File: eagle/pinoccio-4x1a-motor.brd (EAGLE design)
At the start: 25.4 x 43.2 mm, 3 parts

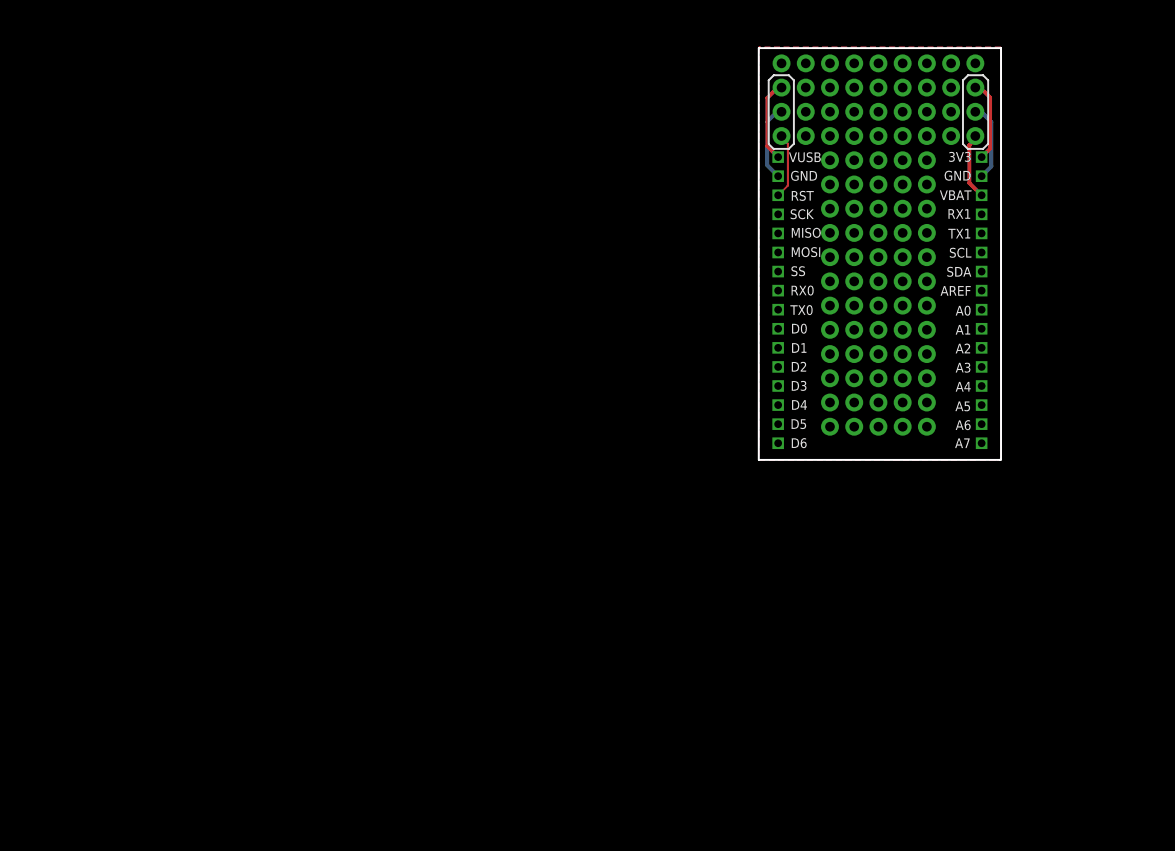
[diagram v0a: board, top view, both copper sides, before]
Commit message: First commit of new shield.
Main components added, no signals.
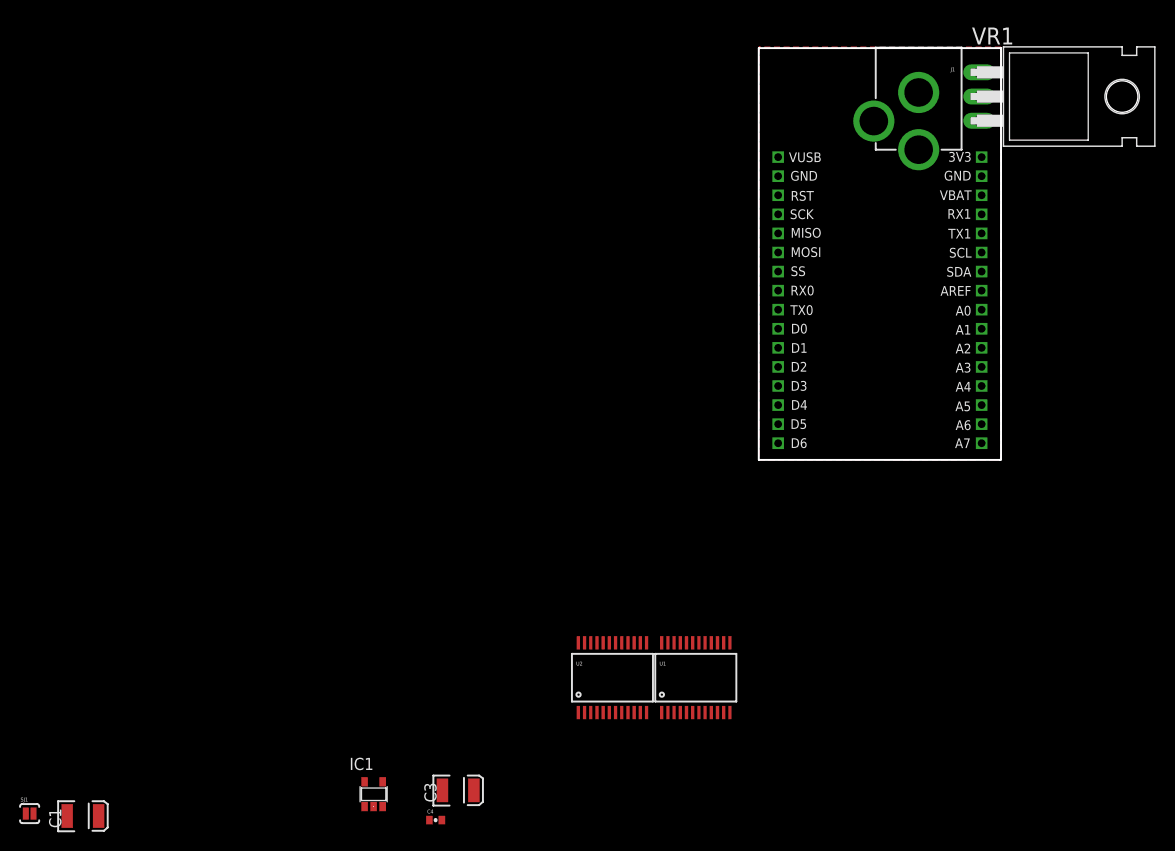
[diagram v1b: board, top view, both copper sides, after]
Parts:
- removed U$1: PROTO, Pinoccio:1X1PROTO
- added C1, C3: 10uf , 20V, SparkFun:EIA3528
- added C4: 0.1uF, SparkFun:0402-CAP
- added IC1: 74LVC1G04DBV, 74xx-little-de:SOT23-5
- added J1: POWER_JACKPTH, SparkFun-Connectors:POWER_JACK_PTH
- added SJ1: SOLDERJUMPERNC2, SparkFun-Passives:SJ_2S-NOTRACE
- added U1, U2: TB6621FNG, SparkFun:SSOP24
- added VR1: LF60ABV, linear:TO220H
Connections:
- new net N$1: C1.A, C3.A, C4.2, VR1.3
- new net N$2: IC1.2, U1.21
- new net N$3: IC1.4, SJ1.1, U1.22
- new net N$4: SJ1.2
- new net VCC: IC1.5
- net GND: now also C1.C, C3.C, C4.1, IC1.3, VR1.1; no longer U$1.53, U$1.77, U$1.P-GND, U$1.P-GND2
- net RESET: no longer U$1.P-RESET
- net VBAT-AE: no longer U$1.P-VBAT
- net VCC-AE: no longer U$1.P-VCC
- net VUSB: no longer U$1.P-VUSB
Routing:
- net GND: track 16.3 -> 0.00 mm
- net VUSB: track 8.62 -> 0.00 mm
- net VCC-AE: track 8.60 -> 0.00 mm
- net VBAT-AE: track 7.01 -> 0.00 mm
- net RESET: track 6.90 -> 0.00 mm
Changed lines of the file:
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@@
 <?xml version="1.0" encoding="utf-8"?>
 <!DOCTYPE eagle SYSTEM "eagle.dtd">
-<eagle version="6.2">
+<eagle version="6.4">
 <drawing>
 <settings>
@@
 <setting verticaltext="up"/>
 </settings>
-<grid distance="1" unitdist="mil" unit="mil" style="lines" multiple="1" display="yes" altdistance="0.001" altunitdist="inch" altunit="inch"/>
+<grid distance="0.01" unitdist="inch" unit="inch" style="lines" multiple="1" display="yes" altdistance="0.001" altunitdist="inch" altunit="mil"/>
 <layers>
 <layer number="1" name="Top" color="4" fill="1" visible="yes" active="yes"/>
@@
 <wire x1="0.0254" y1="7.62" x2="25.2984" y2="7.62" width="0.2032" layer="20"/>
 <wire x1="25.2984" y1="7.62" x2="25.3238" y2="7.6454" width="0.2032" layer="20"/>
-<wire x1="1.5748" y1="47.9552" x2="3.1496" y2="47.9552" width="0.2032" layer="21"/>
-<wire x1="3.1496" y1="47.9552" x2="3.683" y2="47.4218" width="0.2032" layer="21"/>
-<wire x1="3.683" y1="47.4218" x2="3.683" y2="40.767" width="0.2032" layer="21"/>
-<wire x1="3.683" y1="40.767" x2="3.1496" y2="40.2336" width="0.2032" layer="21"/>
-<wire x1="3.1496" y1="40.2336" x2="1.5494" y2="40.2336" width="0.2032" layer="21"/>
-<wire x1="1.5494" y1="40.2336" x2="1.0414" y2="40.7416" width="0.2032" layer="21"/>
-<wire x1="1.0414" y1="40.7416" x2="1.0414" y2="47.4218" width="0.2032" layer="21"/>
-<wire x1="1.0414" y1="47.4218" x2="1.5748" y2="47.9552" width="0.2032" layer="21"/>
-<wire x1="21.9456" y1="47.9552" x2="23.5204" y2="47.9552" width="0.2032" layer="21"/>
-<wire x1="23.5204" y1="47.9552" x2="24.0538" y2="47.4218" width="0.2032" layer="21"/>
-<wire x1="24.0538" y1="47.4218" x2="24.0538" y2="40.767" width="0.2032" layer="21"/>
-<wire x1="24.0538" y1="40.767" x2="23.5204" y2="40.2336" width="0.2032" layer="21"/>
-<wire x1="23.5204" y1="40.2336" x2="21.9202" y2="40.2336" width="0.2032" layer="21"/>
-<wire x1="21.9202" y1="40.2336" x2="21.4122" y2="40.7416" width="0.2032" layer="21"/>
-<wire x1="21.4122" y1="40.7416" x2="21.4122" y2="47.4218" width="0.2032" layer="21"/>
-<wire x1="21.4122" y1="47.4218" x2="21.9456" y2="47.9552" width="0.2032" layer="21"/>
 </plain>
 <attributes>
@@
 </class>
 </classes>
-<designrules>
+<designrules name="default">
 <description language="de">&lt;b&gt;EAGLE Design Rules&lt;/b&gt;
 &lt;p&gt;
@@
 <element name="JP-R" library="Pinoccio" package="1X16_2MM" value="M162MM" x="23.368" y="39.37" locked="yes" smashed="yes" rot="R270"/>
 <element name="JP-L" library="Pinoccio" package="1X16_2MM" value="M162MM" x="2.032" y="39.37" locked="yes" smashed="yes" rot="R270"/>
-<element name="U$1" library="Pinoccio" package="1X1PROTO" value="PROTO" x="7.4676" y="8.5598"/>
+<element name="U1" library="SparkFun" package="SSOP24" value="TB6621FNG" x="-6.604" y="-15.2146"/>
+<element name="U2" library="SparkFun" package="SSOP24" value="TB6621FNG" x="-15.3416" y="-15.2146"/>
+<element name="VR1" library="linear" package="TO220H" value="LF60ABV" x="33.274" y="45.72" rot="R270"/>
+<element name="C4" library="SparkFun" package="0402-CAP" value="0.1uF" x="-33.8836" y="-30.1498"/>
+<element name="C3" library="SparkFun" package="EIA3528" value="10uf , 20V" x="-31.5214" y="-27.0256"/>
+<element name="IC1" library="74xx-little-de" package="SOT23-5" value="74LVC1G04DBV" x="-40.386" y="-27.432"/>
+<element name="C1" library="SparkFun" package="EIA3528" value="10uf , 20V" x="-70.866" y="-29.718"/>
+<element name="J1" library="SparkFun-Connectors" package="POWER_JACK_PTH" value="POWER_JACKPTH" x="16.764" y="53.848" rot="R180"/>
+<element name="SJ1" library="SparkFun-Passives" package="SJ_2S-NOTRACE" value="SOLDERJUMPERNC2" x="-76.454" y="-29.464"/>
 </elements>
 <signals>
@@
 <contactref element="JP-L" pad="P$2"/>
 <contactref element="JP-R" pad="P$2"/>
-<contactref element="U$1" pad="P-GND"/>
-<contactref element="U$1" pad="P-GND2"/>
-<contactref element="U$1" pad="77"/>
-<contactref element="U$1" pad="53"/>
-<wire x1="2.032" y1="37.37" x2="0.889" y2="38.513" width="0.4064" layer="16"/>
-<wire x1="0.889" y1="38.513" x2="0.889" y2="43.1038" width="0.4064" layer="16"/>
-<wire x1="0.889" y1="43.1038" x2="1.905" y2="44.1198" width="0.4064" layer="16"/>
-<wire x1="1.905" y1="44.1198" x2="2.3876" y2="44.1198" width="0.4064" layer="16"/>
-<wire x1="23.368" y1="37.37" x2="24.384" y2="38.386" width="0.4064" layer="16"/>
-<wire x1="24.384" y1="38.386" x2="24.384" y2="43.053" width="0.4064" layer="16"/>
-<wire x1="24.384" y1="43.053" x2="23.3172" y2="44.1198" width="0.4064" layer="16"/>
-<wire x1="23.3172" y1="44.1198" x2="22.7076" y2="44.1198" width="0.4064" layer="16"/>
 <polygon width="0.4064" layer="1">
 <vertex x="0.0762" y="50.9524"/>
@@
 <vertex x="0.1016" y="50.8762"/>
 </polygon>
-<wire x1="12.5476" y1="33.9598" x2="12.5476" y2="44.1198" width="0" layer="19" extent="1-1"/>
-<wire x1="2.3876" y1="44.1198" x2="12.5476" y2="44.1198" width="0" layer="19" extent="1-1"/>
+<contactref element="IC1" pad="3"/>
+<contactref element="C4" pad="1"/>
+<contactref element="VR1" pad="1"/>
+<contactref element="C3" pad="C"/>
+<contactref element="C1" pad="C"/>
+<wire x1="-39.436" y1="-28.722" x2="-72.516" y2="-29.718" width="0" layer="19" extent="1-1"/>
+<wire x1="-34.5336" y1="-30.1498" x2="-39.436" y2="-28.722" width="0" layer="19" extent="1-1"/>
+<wire x1="-33.1714" y1="-27.0256" x2="-34.5336" y2="-30.1498" width="0" layer="19" extent="1-1"/>
+<wire x1="2.032" y1="37.37" x2="-33.1714" y2="-27.0256" width="0" layer="19" extent="1-1"/>
+<wire x1="23.368" y1="37.37" x2="2.032" y2="37.37" width="0" layer="19" extent="1-1"/>
+<wire x1="23.114" y1="48.26" x2="23.368" y2="37.37" width="0" layer="19" extent="1-1"/>
 </signal>
 <signal name="MOSI">
@@
 <signal name="VUSB">
 <contactref element="JP-L" pad="P$1"/>
-<contactref element="U$1" pad="P-VUSB"/>
-<wire x1="2.032" y1="39.37" x2="0.889" y2="40.513" width="0.4064" layer="1"/>
-<wire x1="0.889" y1="40.513" x2="0.889" y2="45.5676" width="0.4064" layer="1"/>
-<wire x1="0.889" y1="45.5676" x2="1.9812" y2="46.6598" width="0.4064" layer="1"/>
-<wire x1="1.9812" y1="46.6598" x2="2.3876" y2="46.6598" width="0.4064" layer="1"/>
 </signal>
 <signal name="VBAT-AE">
 <contactref element="JP-R" pad="P$3"/>
-<contactref element="U$1" pad="P-VBAT"/>
-<wire x1="23.368" y1="35.37" x2="22.0726" y2="36.6654" width="0.4064" layer="1"/>
-<wire x1="22.0726" y1="36.6654" x2="22.0726" y2="40.6146" width="0.4064" layer="1"/>
-<wire x1="22.0726" y1="40.6146" x2="22.7076" y2="41.2496" width="0.4064" layer="1"/>
-<wire x1="22.7076" y1="41.2496" x2="22.7076" y2="41.5798" width="0.4064" layer="1"/>
 </signal>
 <signal name="SSN">
@@
 <signal name="RESET">
 <contactref element="JP-L" pad="P$3"/>
-<contactref element="U$1" pad="P-RESET"/>
-<wire x1="2.032" y1="35.37" x2="3.048" y2="36.386" width="0.2032" layer="1"/>
-<wire x1="3.048" y1="36.386" x2="3.048" y2="40.7924" width="0.2032" layer="1"/>
-<wire x1="3.048" y1="40.7924" x2="2.3876" y2="41.4528" width="0.2032" layer="1"/>
-<wire x1="2.3876" y1="41.4528" x2="2.3876" y2="41.5798" width="0.2032" layer="1"/>
 </signal>
 <signal name="A0">
@@
 <signal name="VCC-AE">
 <contactref element="JP-R" pad="P$1"/>
-<contactref element="U$1" pad="P-VCC"/>
-<wire x1="23.368" y1="39.37" x2="24.257" y2="40.259" width="0.4064" layer="1"/>
-<wire x1="24.257" y1="40.259" x2="24.257" y2="45.6184" width="0.4064" layer="1"/>
-<wire x1="24.257" y1="45.6184" x2="23.2156" y2="46.6598" width="0.4064" layer="1"/>
-<wire x1="23.2156" y1="46.6598" x2="22.7076" y2="46.6598" width="0.4064" layer="1"/>
 </signal>
 <signal name="VIN">
 </signal>
+<signal name="VCC">
+<contactref element="IC1" pad="5"/>
+</signal>
+<signal name="N$1">
+<contactref element="VR1" pad="3"/>
+<contactref element="C4" pad="2"/>
+<contactref element="C3" pad="A"/>
+<contactref element="C1" pad="A"/>
+<wire x1="-33.2336" y1="-30.1498" x2="-69.216" y2="-29.718" width="0" layer="19" extent="1-1"/>
+<wire x1="-29.8714" y1="-27.0256" x2="-33.2336" y2="-30.1498" width="0" layer="19" extent="1-1"/>
+<wire x1="23.114" y1="43.18" x2="-29.8714" y2="-27.0256" width="0" layer="19" extent="1-1"/>
+</signal>
+<signal name="N$3">
+<contactref element="U1" pad="22"/>
+<contactref element="IC1" pad="4"/>
+<contactref element="SJ1" pad="1"/>
+<wire x1="-39.436" y1="-26.132" x2="-76.8549" y2="-29.464" width="0" layer="19" extent="1-1"/>
+<wire x1="-8.879" y1="-11.5586" x2="-39.436" y2="-26.132" width="0" layer="19" extent="1-1"/>
+</signal>
+<signal name="N$2">
+<contactref element="U1" pad="21"/>
+<contactref element="IC1" pad="2"/>
+<wire x1="-8.229" y1="-11.5586" x2="-40.386" y2="-28.722" width="0" layer="19" extent="1-1"/>
+</signal>
+<signal name="N$4">
+<contactref element="SJ1" pad="2"/>
+</signal>
 </signals>
